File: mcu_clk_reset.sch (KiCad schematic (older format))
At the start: 52 parts, among them J4 20021121-00010C4LF, J5 M20-8762042, Q3 BSS214NW, Q4 BSS214NW, Q5 BSS214NW, Q6 BSS214NW, U4 IS25WP032D, U5 FE310-G002, X1 KX2132709Z, Y1 TSX-3225 16.0000MF18X-AC0

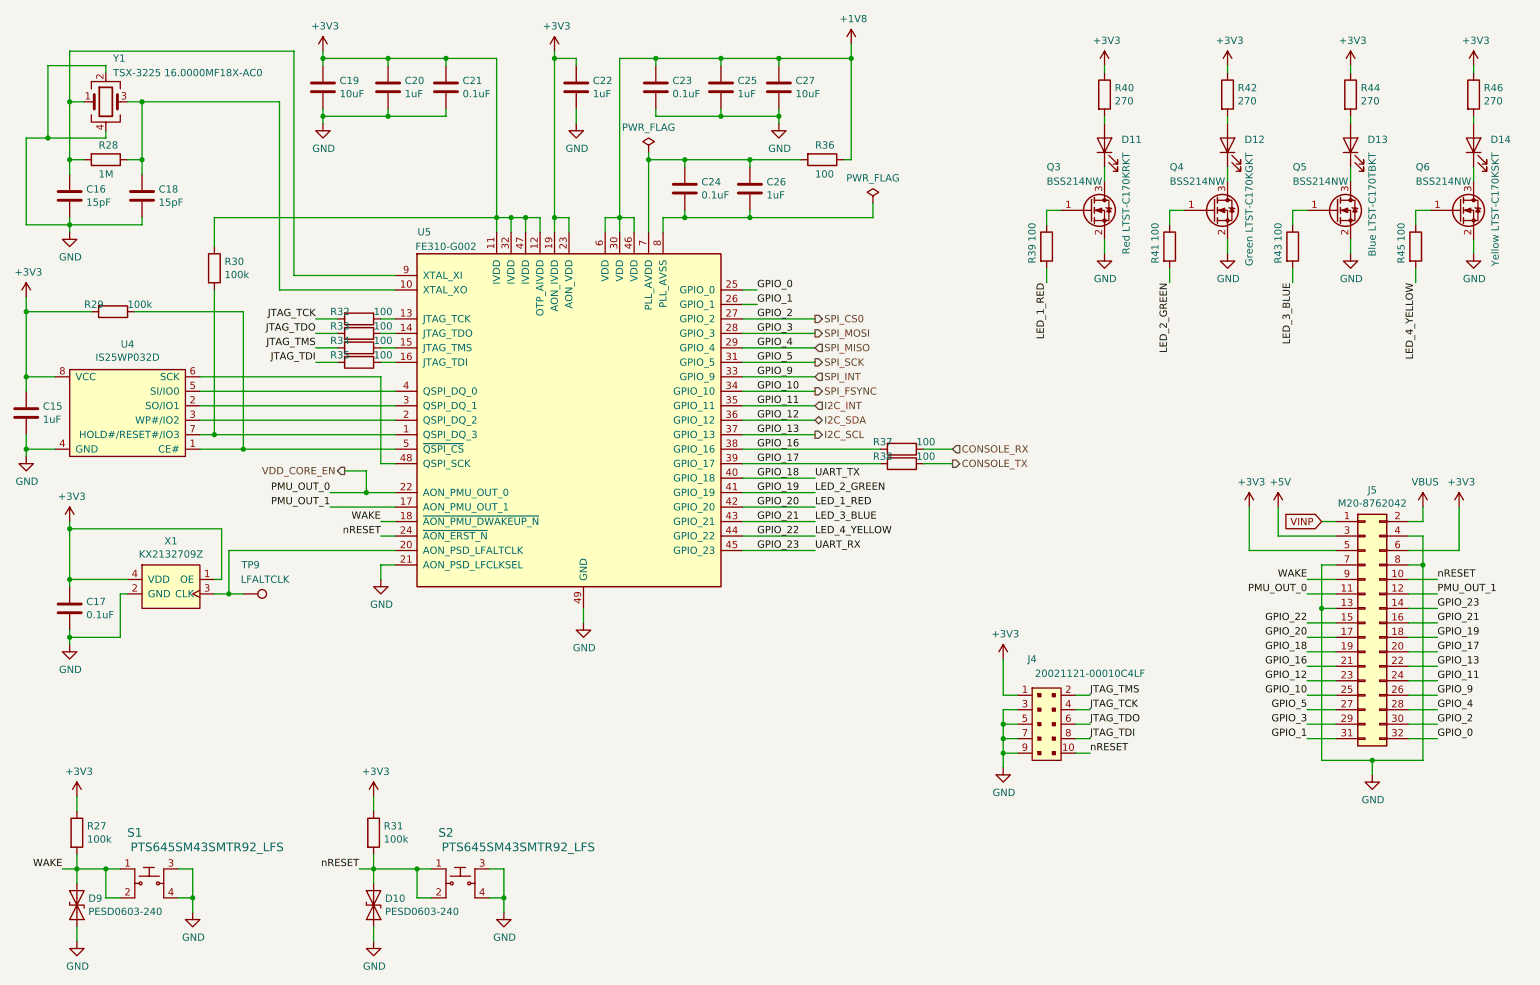
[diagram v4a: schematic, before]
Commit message: Remap main header pins
Allows for better use of board estate.
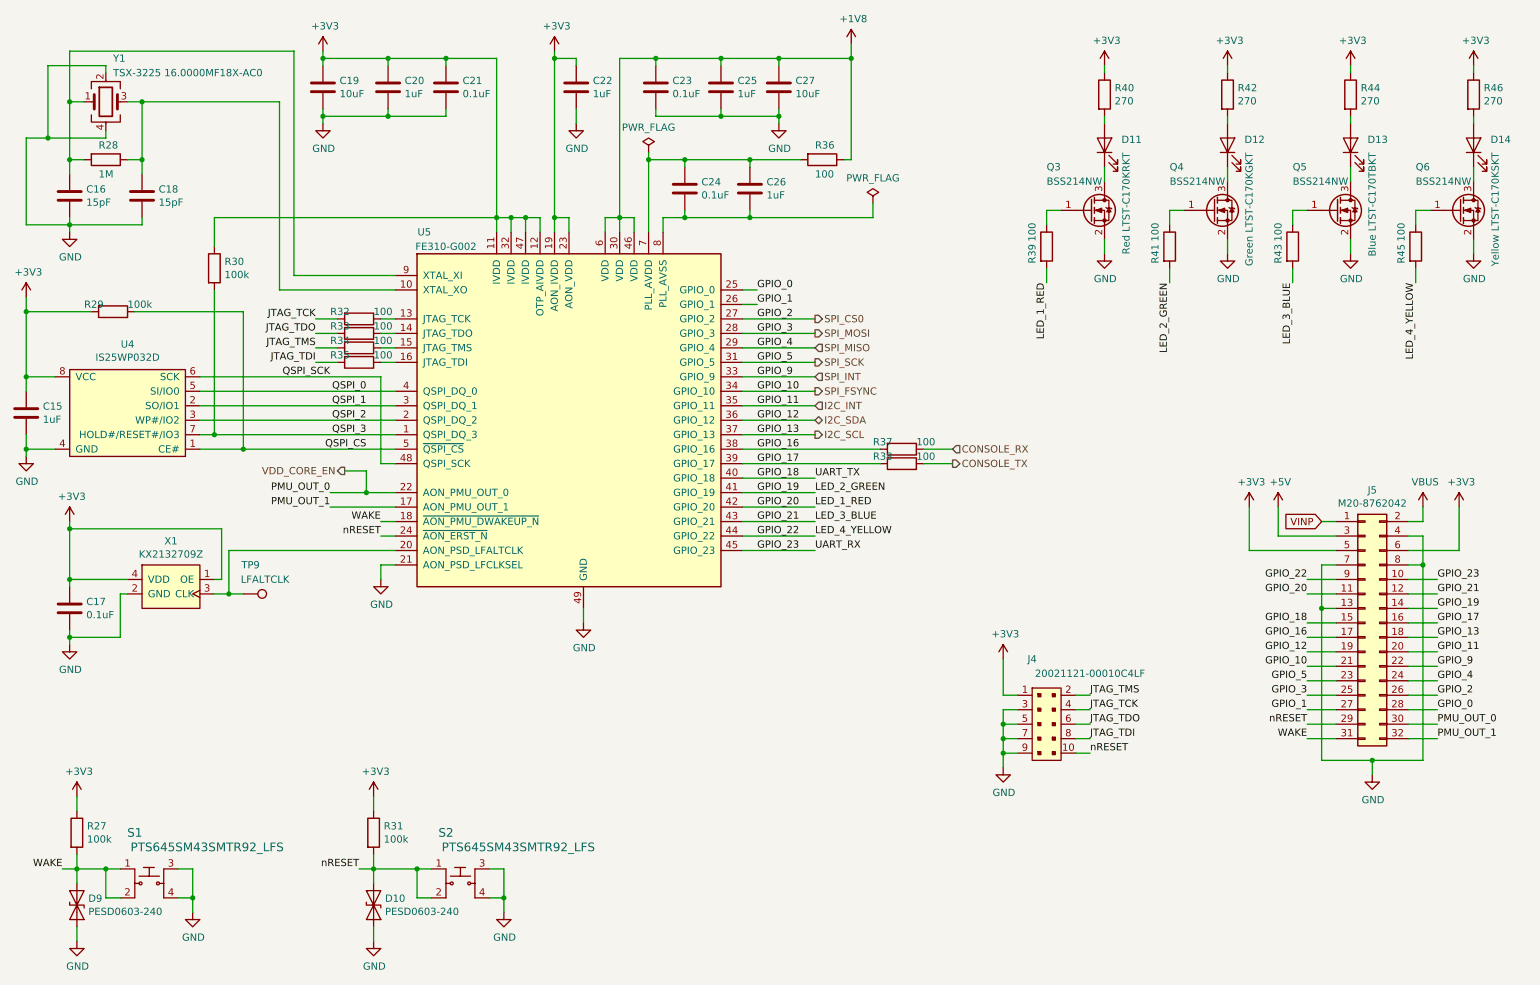
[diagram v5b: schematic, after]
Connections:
- net GPIO_0: now also J5.28 (Pin_28); no longer J5.32 (Pin_32)
- net GPIO_1: now also J5.27 (Pin_27); no longer J5.31 (Pin_31)
- net GPIO_16: now also J5.17 (Pin_17); no longer J5.21 (Pin_21)
- net GPIO_17: now also J5.16 (Pin_16); no longer J5.20 (Pin_20)
- net GPIO_18: now also J5.15 (Pin_15); no longer J5.19 (Pin_19)
- net GPIO_19: now also J5.14 (Pin_14); no longer J5.18 (Pin_18)
- net GPIO_20: now also J5.11 (Pin_11); no longer J5.17 (Pin_17)
- net GPIO_21: now also J5.12 (Pin_12); no longer J5.16 (Pin_16)
- net GPIO_22: now also J5.9 (Pin_9); no longer J5.15 (Pin_15)
- net GPIO_23: now also J5.10 (Pin_10); no longer J5.14 (Pin_14)
- net I2C_INT: now also J5.20 (Pin_20); no longer J5.24 (Pin_24)
- net I2C_SCL: now also J5.18 (Pin_18); no longer J5.22 (Pin_22)
- net I2C_SDA: now also J5.19 (Pin_19); no longer J5.23 (Pin_23)
- net PMU_OUT_1: now also J5.32 (Pin_32); no longer J5.12 (Pin_12)
- net SPI_CS0: now also J5.26 (Pin_26); no longer J5.30 (Pin_30)
- net SPI_FSYNC: now also J5.21 (Pin_21); no longer J5.25 (Pin_25)
- net SPI_INT: now also J5.22 (Pin_22); no longer J5.26 (Pin_26)
- net SPI_MISO: now also J5.24 (Pin_24); no longer J5.28 (Pin_28)
- net SPI_MOSI: now also J5.25 (Pin_25); no longer J5.29 (Pin_29)
- net SPI_SCK: now also J5.23 (Pin_23); no longer J5.27 (Pin_27)
- net VDD_CORE_EN: now also J5.30 (Pin_30); no longer J5.11 (Pin_11)
- net WAKE: now also J5.31 (Pin_31); no longer J5.9 (Pin_9)
- net nRESET: now also J5.29 (Pin_29); no longer J5.10 (Pin_10)
- net QSPI_3: now reaches R30.2, U4.7 (HOLD#/RESET#/IO3), U5.1 (QSPI_DQ_3)
- net QSPI_2: now reaches U4.3 (WP#/IO2), U5.2 (QSPI_DQ_2)
- net QSPI_1: now reaches U4.2 (SO/IO1), U5.3 (QSPI_DQ_1)
- net QSPI_0: now reaches U4.5 (SI/IO0), U5.4 (QSPI_DQ_0)
- net QSPI_SCK: now reaches U4.6 (SCK), U5.48 (QSPI_SCK)
- net QSPI_CS: now reaches R29.1, U4.1 (CE#), U5.5 (~QSPI_CS)
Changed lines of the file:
@@
 Wire Wire Line
 	1000 6000 1000 6100
-Text Label 9500 4500 2    50   ~ 0
+Text Label 9500 5600 2    50   ~ 0
 WAKE
-Text Label 10400 4500 0    50   ~ 0
+Text Label 9500 5500 2    50   ~ 0
 nRESET
 Wire Wire Line
@@
 Wire Wire Line
 	5700 2600 5600 2600
-Text Label 9500 5300 2    50   ~ 0
+Text Label 9500 5100 2    50   ~ 0
 GPIO_10
-Text Label 10400 5300 0    50   ~ 0
+Text Label 10400 5100 0    50   ~ 0
 GPIO_9
 Wire Wire Line
@@
 Text Label 5700 3700 0    50   ~ 0
 GPIO_17
+Text Label 10400 4800 0    50   ~ 0
+GPIO_17
+Text Label 9500 4900 2    50   ~ 0
+GPIO_16
+Text Label 10400 4900 0    50   ~ 0
+GPIO_13
+Text Label 9500 5000 2    50   ~ 0
+GPIO_12
 Text Label 10400 5000 0    50   ~ 0
-GPIO_17
-Text Label 9500 5100 2    50   ~ 0
-GPIO_16
-Text Label 10400 5100 0    50   ~ 0
-GPIO_13
+GPIO_11
 Text Label 9500 5200 2    50   ~ 0
-GPIO_12
+GPIO_5
 Text Label 10400 5200 0    50   ~ 0
-GPIO_11
+GPIO_4
+Text Label 9500 5300 2    50   ~ 0
+GPIO_3
+Text Label 10400 5300 0    50   ~ 0
+GPIO_2
 Text Label 9500 5400 2    50   ~ 0
-GPIO_5
+GPIO_1
 Text Label 10400 5400 0    50   ~ 0
-GPIO_4
-Text Label 9500 5500 2    50   ~ 0
-GPIO_3
+GPIO_0
 Text Label 10400 5500 0    50   ~ 0
-GPIO_2
-Text Label 9500 5600 2    50   ~ 0
-GPIO_1
+PMU_OUT_0
 Text Label 10400 5600 0    50   ~ 0
-GPIO_0
-Text Label 9500 4600 2    50   ~ 0
-PMU_OUT_0
-Text Label 10400 4600 0    50   ~ 0
 PMU_OUT_1
 Wire Wire Line
@@
 Text Label 5700 4300 0    50   ~ 0
 GPIO_23
-Text Label 9500 5000 2    50   ~ 0
+Text Label 9500 4800 2    50   ~ 0
 GPIO_18
-Text Label 10400 4900 0    50   ~ 0
+Text Label 10400 4700 0    50   ~ 0
 GPIO_19
-Text Label 9500 4900 2    50   ~ 0
+Text Label 9500 4600 2    50   ~ 0
 GPIO_20
-Text Label 10400 4800 0    50   ~ 0
+Text Label 10400 4600 0    50   ~ 0
 GPIO_21
-Text Label 9500 4800 2    50   ~ 0
+Text Label 9500 4500 2    50   ~ 0
 GPIO_22
-Text Label 10400 4700 0    50   ~ 0
+Text Label 10400 4500 0    50   ~ 0
 GPIO_23
 Wire Wire Line
@@
 Wire Wire Line
 	9100 4300 9700 4300
+Text Label 3000 3200 2    50   ~ 0
+QSPI_0
+Text Label 3000 3300 2    50   ~ 0
+QSPI_1
+Text Label 3000 3400 2    50   ~ 0
+QSPI_2
+Text Label 3000 3500 2    50   ~ 0
+QSPI_3
+Text Label 3000 3600 2    50   ~ 0
+QSPI_CS
+Text Label 2750 3100 2    50   ~ 0
+QSPI_SCK
 $EndSCHEMATC

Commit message: Re-annotated all elements
This is a step to prepare for a change from 0805 to 0603 components. Not
critical but nice to have them in order.
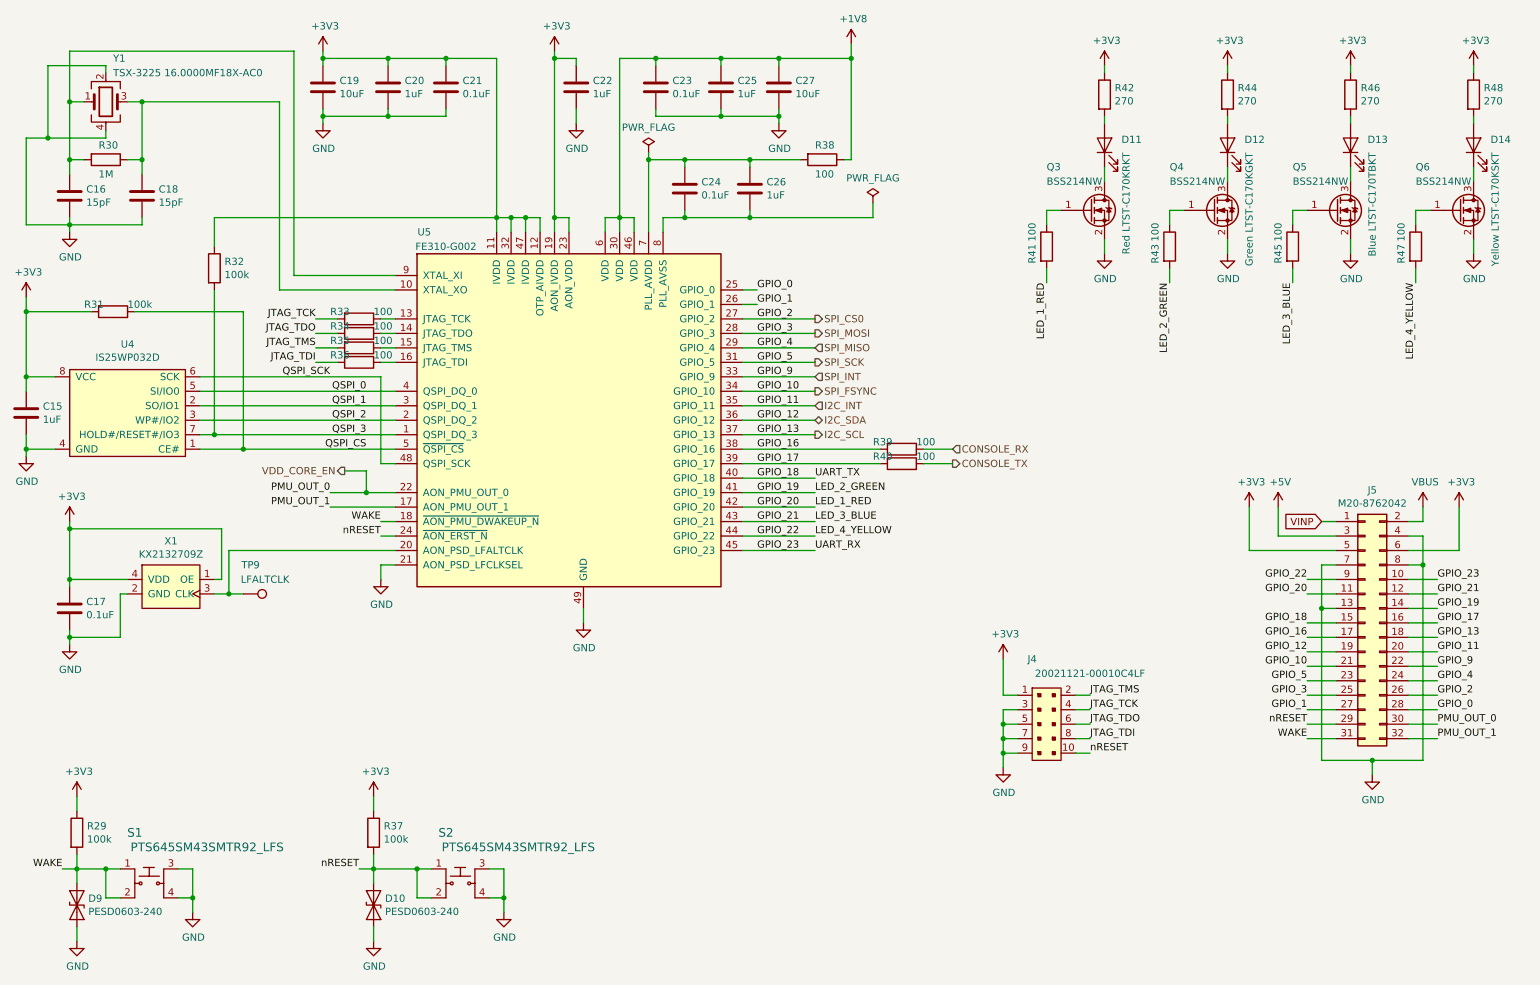
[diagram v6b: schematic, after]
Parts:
- renumbered R27 to R29, R28 to R30, R29 to R31, R30 to R32, R32 to R33, R33 to R34, R34 to R35, R35 to R36, R31 to R37, R36 to R38, R37 to R39, R38 to R40, R39 to R41, R40 to R42, R41 to R43, R42 to R44, R43 to R45, R44 to R46, R45 to R47, R46 to R48

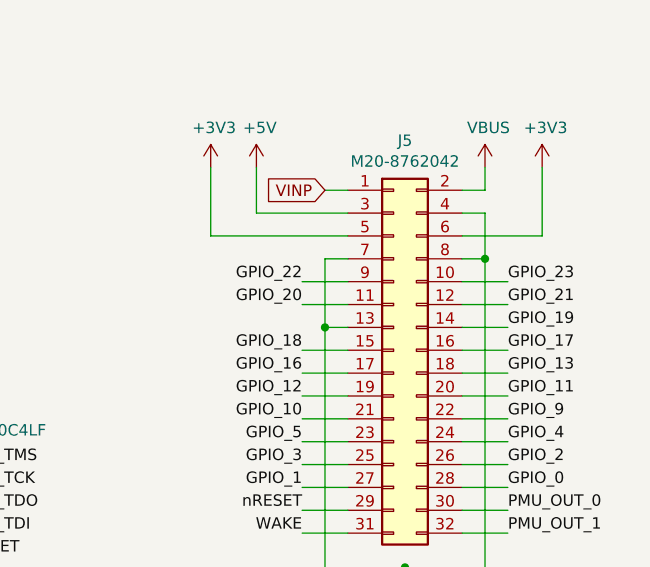
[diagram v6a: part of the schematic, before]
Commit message: Use 0603 components, on both sides, route header
This decision was due to the current placement overcrowded and to the
fact that successful routing on one side was uncertain.
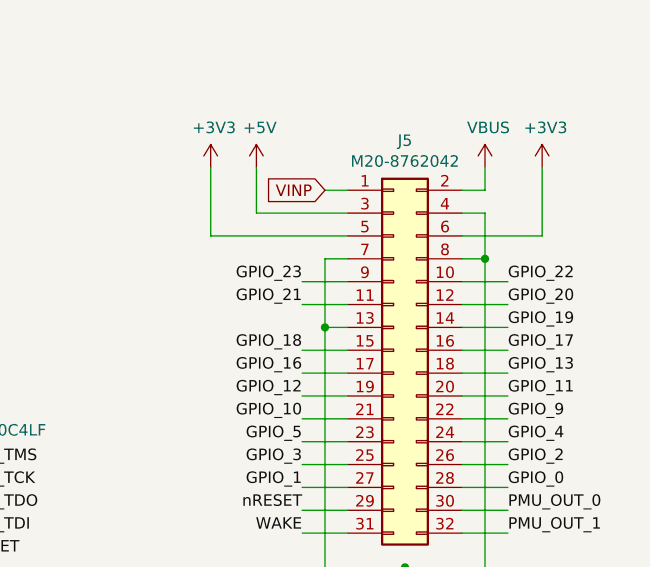
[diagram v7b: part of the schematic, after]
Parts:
- C15, C16, C17, C18, C19, C20, C21, C22, C23, C24, C25, C26, C27: footprint Capacitor_SMD:C_0805_2012Metric_Pad1.15x1.40mm_HandSolder -> Capacitor_SMD:C_0603_1608Metric_Pad1.05x0.95mm_HandSolder
- R29, R30, R31, R32, R33, R34, R35, R36, R37, R38, R39, R40, R41, R42, R43, R44, R45, R46, R47, R48: footprint Resistor_SMD:R_0805_2012Metric_Pad1.15x1.40mm_HandSolder -> Resistor_SMD:R_0603_1608Metric_Pad1.05x0.95mm_HandSolder
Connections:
- net GPIO_20: now also J5.12 (Pin_12); no longer J5.11 (Pin_11)
- net GPIO_21: now also J5.11 (Pin_11); no longer J5.12 (Pin_12)
- net GPIO_22: now also J5.10 (Pin_10); no longer J5.9 (Pin_9)
- net GPIO_23: now also J5.9 (Pin_9); no longer J5.10 (Pin_10)
